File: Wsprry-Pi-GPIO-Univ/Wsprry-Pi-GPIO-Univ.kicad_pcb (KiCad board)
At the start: 2 copper layers, 65 x 30 mm, 25 parts, among them J11 GPIO, J81 Conn_01x04, J82 Conn_01x04, J83 SMA, SW11 Switch, U51 GVA-84

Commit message: Cleanup due to lost libraries
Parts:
- C12, C51: footprint Capacitor_SMD:C_0603_1608Metric -> Wsprry Pi:C_0603_1608Metric
- C52, C53: footprint Capacitor_SMD:C_0402_1005Metric -> Wsprry Pi:C_0402_1005Metric
- C54, C55: footprint Capacitor_SMD:C_0805_2012Metric -> Wsprry Pi:C_0805_2012Metric
- D11: footprint LED_SMD:LED_0603_1608Metric -> Wsprry Pi:LED_0603_1608Metric
- FB11, FB51: footprint Inductor_SMD:L_0603_1608Metric -> Wsprry Pi:L_0603_1608Metric
- J11: footprint Connector_PinSocket_2.54mm:PinSocket_2x20_P2.54mm_Vertical -> Wsprry Pi:PinSocket_2x20_P2.54mm_Vertical
- J81, J82: footprint Connector_PinSocket_2.54mm:PinSocket_1x04_P2.54mm_Vertical -> Wsprry Pi:PinSocket_1x04_P2.54mm_Vertical
- MH1, MH2, MH3, MH4: footprint MountingHole:MountingHole_2.7mm_M2.5 -> Wsprry Pi:MountingHole_2.7mm_M2.5
- R11, R41, R42, R43: footprint Resistor_SMD:R_0603_1608Metric -> Wsprry Pi:R_0603_1608Metric
- R51: footprint Resistor_SMD:R_0805_2012Metric -> Wsprry Pi:R_0805_2012Metric
- U51: footprint Package_TO_SOT_SMD:SOT-89-3 -> Wsprry Pi:SOT-89-3
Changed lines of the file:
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@@
 		)
 		(embedded_fonts no)
-		(model "${KIPRJMOD}/EASYEDA_MODELS/SW-SMD_4P-L5.1-W5.1-P3.70-LS6.5-TL_H1.5.step"
+		(model "${KIPRJMOD}/libraries/3dmodels/vendor/SW-SMD_4P-L5.1-W5.1-P3.70-LS6.5-TL_H1.5.step"
 			(offset
 				(xyz 0 0 0)
@@
 		)
 	)
-	(footprint "LED_SMD:LED_0603_1608Metric"
+	(footprint "Wsprry Pi:LED_0603_1608Metric"
 		(layer "F.Cu")
 		(at 104.6225 77.58)
@@
 		)
 		(embedded_fonts no)
-		(model "${KICAD9_3DMODEL_DIR}/LED_SMD.3dshapes/LED_0603_1608Metric.step"
+		(model "${KIPRJMOD}/libraries/3dmodels/LED_SMD.3dshapes/LED_0603_1608Metric.step"
 			(offset
 				(xyz 0 0 0)
@@
 		)
 	)
-	(footprint "Capacitor_SMD:C_0805_2012Metric"
+	(footprint "Wsprry Pi:C_0805_2012Metric"
 		(layer "F.Cu")
 		(at 146.694973 83.11)
@@
 		)
 		(embedded_fonts no)
-		(model "${KICAD9_3DMODEL_DIR}/Capacitor_SMD.3dshapes/C_0805_2012Metric.step"
+		(model "${KIPRJMOD}/libraries/3dmodels/Capacitor_SMD.3dshapes/C_0805_2012Metric.step"
 			(offset
 				(xyz 0 0 0)
@@
 		)
 	)
-	(footprint "MountingHole:MountingHole_2.7mm_M2.5"
+	(footprint "Wsprry Pi:MountingHole_2.7mm_M2.5"
 		(layer "F.Cu")
 		(at 161.5 73.5)
@@
 		)
 		(embedded_fonts no)
-		(model "${KIPRJMOD}/EASYEDA_MODELS/SMA-TH_5P-L14.5-W6.0-H9.6_BWSMA-KWE-Z001.step"
+		(model "${KIPRJMOD}/libraries/3dmodels/vendor/SMA-TH_5P-L14.5-W6.0-H9.6_BWSMA-KWE-Z001.step"
 			(offset
 				(xyz 4.315 0 -3.5)
@@
 		)
 	)
-	(footprint "Inductor_SMD:L_0603_1608Metric"
+	(footprint "Wsprry Pi:L_0603_1608Metric"
 		(layer "F.Cu")
 		(at 107.581 77.58)
@@
 		)
 		(embedded_fonts no)
-		(model "${KICAD9_3DMODEL_DIR}/Inductor_SMD.3dshapes/L_0603_1608Metric.step"
+		(model "${KIPRJMOD}/libraries/3dmodels/Inductor_SMD.3dshapes/L_0603_1608Metric.step"
 			(offset
 				(xyz 0 0 0)
@@
 		)
 	)
-	(footprint "Capacitor_SMD:C_0402_1005Metric"
+	(footprint "Wsprry Pi:C_0402_1005Metric"
 		(layer "F.Cu")
 		(at 142.88 87.605 90)
@@
 		)
 		(embedded_fonts no)
-		(model "${KICAD9_3DMODEL_DIR}/Capacitor_SMD.3dshapes/C_0402_1005Metric.step"
+		(model "${KIPRJMOD}/libraries/3dmodels/Capacitor_SMD.3dshapes/C_0402_1005Metric.step"
 			(offset
 				(xyz 0 0 0)
@@
 		)
 	)
-	(footprint "Inductor_SMD:L_0603_1608Metric"
+	(footprint "Wsprry Pi:L_0603_1608Metric"
 		(layer "F.Cu")
 		(at 138.5425 88.0875)
@@
 		)
 		(embedded_fonts no)
-		(model "${KICAD9_3DMODEL_DIR}/Inductor_SMD.3dshapes/L_0603_1608Metric.step"
+		(model "${KIPRJMOD}/libraries/3dmodels/Inductor_SMD.3dshapes/L_0603_1608Metric.step"
 			(offset
 				(xyz 0 0 0)
@@
 		)
 	)
-	(footprint "Resistor_SMD:R_0603_1608Metric"
+	(footprint "Wsprry Pi:R_0603_1608Metric"
 		(layer "F.Cu")
 		(at 143.514973 81.648 180)
@@
 		)
 		(embedded_fonts no)
-		(model "${KICAD9_3DMODEL_DIR}/Resistor_SMD.3dshapes/R_0603_1608Metric.step"
+		(model "${KIPRJMOD}/libraries/3dmodels/Resistor_SMD.3dshapes/R_0603_1608Metric.step"
 			(offset
 				(xyz 0 0 0)
@@
 		(embedded_fonts no)
 	)
-	(footprint "Resistor_SMD:R_0805_2012Metric"
+	(footprint "Wsprry Pi:R_0805_2012Metric"
 		(layer "F.Cu")
 		(at 145.04 88.0875)
@@
 		)
 		(embedded_fonts no)
-		(model "${KICAD9_3DMODEL_DIR}/Resistor_SMD.3dshapes/R_0805_2012Metric.step"
+		(model "${KIPRJMOD}/libraries/3dmodels/Resistor_SMD.3dshapes/R_0805_2012Metric.step"
 			(offset
 				(xyz 0 0 0)
@@
 		)
 	)
-	(footprint "MountingHole:MountingHole_2.7mm_M2.5"
+	(footprint "Wsprry Pi:MountingHole_2.7mm_M2.5"
 		(layer "F.Cu")
 		(at 103.5 96.5)
@@
 		(embedded_fonts no)
 	)
-	(footprint "Resistor_SMD:R_0603_1608Metric"
+	(footprint "Wsprry Pi:R_0603_1608Metric"
 		(layer "F.Cu")
 		(at 143.514973 83.109)
@@
 		)
 		(embedded_fonts no)
-		(model "${KICAD9_3DMODEL_DIR}/Resistor_SMD.3dshapes/R_0603_1608Metric.step"
+		(model "${KIPRJMOD}/libraries/3dmodels/Resistor_SMD.3dshapes/R_0603_1608Metric.step"
 			(offset
 				(xyz 0 0 0)
@@
 		)
 	)
-	(footprint "MountingHole:MountingHole_2.7mm_M2.5"
+	(footprint "Wsprry Pi:MountingHole_2.7mm_M2.5"
 		(layer "F.Cu")
 		(at 103.5 73.5)
@@
 		(embedded_fonts no)
 	)
-	(footprint "Resistor_SMD:R_0603_1608Metric"
+	(footprint "Wsprry Pi:R_0603_1608Metric"
 		(layer "F.Cu")
 		(at 141.864973 80.189)
@@
 		)
 		(embedded_fonts no)
-		(model "${KICAD9_3DMODEL_DIR}/Resistor_SMD.3dshapes/R_0603_1608Metric.step"
+		(model "${KIPRJMOD}/libraries/3dmodels/Resistor_SMD.3dshapes/R_0603_1608Metric.step"
 			(offset
 				(xyz 0 0 0)
@@
 		)
 	)
-	(footprint "Capacitor_SMD:C_0603_1608Metric"
+	(footprint "Wsprry Pi:C_0603_1608Metric"
 		(layer "F.Cu")
 		(at 140.7625 87.3125 90)
@@
 		)
 		(embedded_fonts no)
-		(model "${KICAD9_3DMODEL_DIR}/Capacitor_SMD.3dshapes/C_0603_1608Metric.step"
+		(model "${KIPRJMOD}/libraries/3dmodels/Capacitor_SMD.3dshapes/C_0603_1608Metric.step"
 			(offset
 				(xyz 0 0 0)
@@
 		)
 	)
-	(footprint "Package_TO_SOT_SMD:SOT-89-3"
+	(footprint "Wsprry Pi:SOT-89-3"
 		(layer "F.Cu")
 		(at 149.6 86.5875)
@@
 		)
 		(embedded_fonts no)
-		(model "${KICAD9_3DMODEL_DIR}/Package_TO_SOT_SMD.3dshapes/SOT-89-3.step"
+		(model "${KIPRJMOD}/libraries/3dmodels/Package_TO_SOT_SMD.3dshapes/SOT-89-3.step"
 			(offset
 				(xyz 0 0 0)
@@
 		)
 	)
-	(footprint "MountingHole:MountingHole_2.7mm_M2.5"
+	(footprint "Wsprry Pi:MountingHole_2.7mm_M2.5"
 		(layer "F.Cu")
 		(at 161.5 96.5)
@@
 		(embedded_fonts no)
 	)
-	(footprint "Connector_PinSocket_2.54mm:PinSocket_1x04_P2.54mm_Vertical"
+	(footprint "Wsprry Pi:PinSocket_1x04_P2.54mm_Vertical"
 		(layer "F.Cu")
 		(at 144.871658 98.471175 180)
@@
 		)
 		(embedded_fonts no)
-		(model "${KICAD9_3DMODEL_DIR}/Connector_PinSocket_2.54mm.3dshapes/PinSocket_1x04_P2.54mm_Vertical.step"
+		(model "${KIPRJMOD}/libraries/3dmodels/Connector_PinSocket_2.54mm.3dshapes/PinSocket_1x04_P2.54mm_Vertical.step"
 			(offset
 				(xyz 0 0 0)
@@
 		)
 	)
-	(footprint "Capacitor_SMD:C_0402_1005Metric"
+	(footprint "Wsprry Pi:C_0402_1005Metric"
 		(layer "F.Cu")
 		(at 141.96 87.605 90)
@@
 		)
 		(embedded_fonts no)
-		(model "${KICAD9_3DMODEL_DIR}/Capacitor_SMD.3dshapes/C_0402_1005Metric.step"
+		(model "${KIPRJMOD}/libraries/3dmodels/Capacitor_SMD.3dshapes/C_0402_1005Metric.step"
 			(offset
 				(xyz 0 0 0)
@@
 		)
 	)
-	(footprint "Capacitor_SMD:C_0805_2012Metric"
+	(footprint "Wsprry Pi:C_0805_2012Metric"
 		(layer "F.Cu")
 		(at 147.65 90.795 -90)
@@
 		)
 		(embedded_fonts no)
-		(model "${KICAD9_3DMODEL_DIR}/Capacitor_SMD.3dshapes/C_0805_2012Metric.step"
+		(model "${KIPRJMOD}/libraries/3dmodels/Capacitor_SMD.3dshapes/C_0805_2012Metric.step"
 			(offset
 				(xyz 0 0 0)
@@
 		)
 	)
-	(footprint "Resistor_SMD:R_0603_1608Metric"
+	(footprint "Wsprry Pi:R_0603_1608Metric"
 		(layer "F.Cu")
 		(at 101.66 77.58)
@@
 		)
 		(embedded_fonts no)
-		(model "${KICAD9_3DMODEL_DIR}/Resistor_SMD.3dshapes/R_0603_1608Metric.step"
+		(model "${KIPRJMOD}/libraries/3dmodels/Resistor_SMD.3dshapes/R_0603_1608Metric.step"
 			(offset
 				(xyz 0 0 0)
@@
 		)
 	)
-	(footprint "Connector_PinSocket_2.54mm:PinSocket_1x04_P2.54mm_Vertical"
+	(footprint "Wsprry Pi:PinSocket_1x04_P2.54mm_Vertical"
 		(layer "F.Cu")
 		(at 112.851658 98.471175 180)
@@
 		)
 		(embedded_fonts no)
-		(model "${KICAD9_3DMODEL_DIR}/Connector_PinSocket_2.54mm.3dshapes/PinSocket_1x04_P2.54mm_Vertical.step"
+		(model "${KIPRJMOD}/libraries/3dmodels/Connector_PinSocket_2.54mm.3dshapes/PinSocket_1x04_P2.54mm_Vertical.step"
 			(offset
 				(xyz 0 0 0)
@@
 		)
 	)
-	(footprint "Capacitor_SMD:C_0603_1608Metric"
+	(footprint "Wsprry Pi:C_0603_1608Metric"
 		(layer "F.Cu")
 		(at 107.59 79.04 180)
@@
 		)
 		(embedded_fonts no)
-		(model "${KICAD9_3DMODEL_DIR}/Capacitor_SMD.3dshapes/C_0603_1608Metric.step"
+		(model "${KIPRJMOD}/libraries/3dmodels/Capacitor_SMD.3dshapes/C_0603_1608Metric.step"
 			(offset
 				(xyz 0 0 0)
@@
 		)
 	)
-	(footprint "Connector_PinSocket_2.54mm:PinSocket_2x20_P2.54mm_Vertical"
+	(footprint "Wsprry Pi:PinSocket_2x20_P2.54mm_Vertical"
 		(layer "B.Cu")
 		(at 108.37 74.77 -90)
@@
 		)
 		(embedded_fonts no)
-		(model "${KICAD9_3DMODEL_DIR}/Connector_PinSocket_2.54mm.3dshapes/PinSocket_2x20_P2.54mm_Vertical.step"
+		(model "${KIPRJMOD}/libraries/3dmodels/Connector_PinSocket_2.54mm.3dshapes/PinSocket_2x20_P2.54mm_Vertical.step"
 			(offset
 				(xyz 0 0 0)

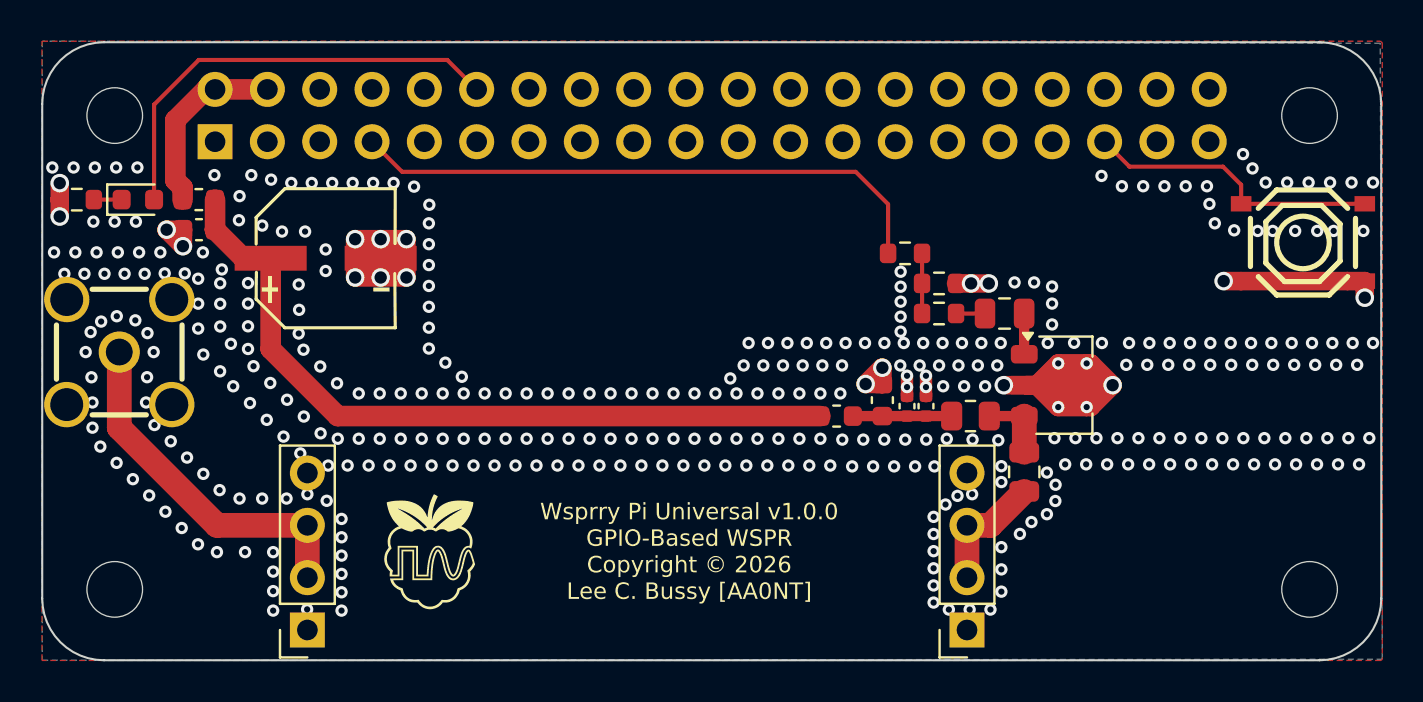
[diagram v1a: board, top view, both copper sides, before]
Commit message: Add GPIO Selector
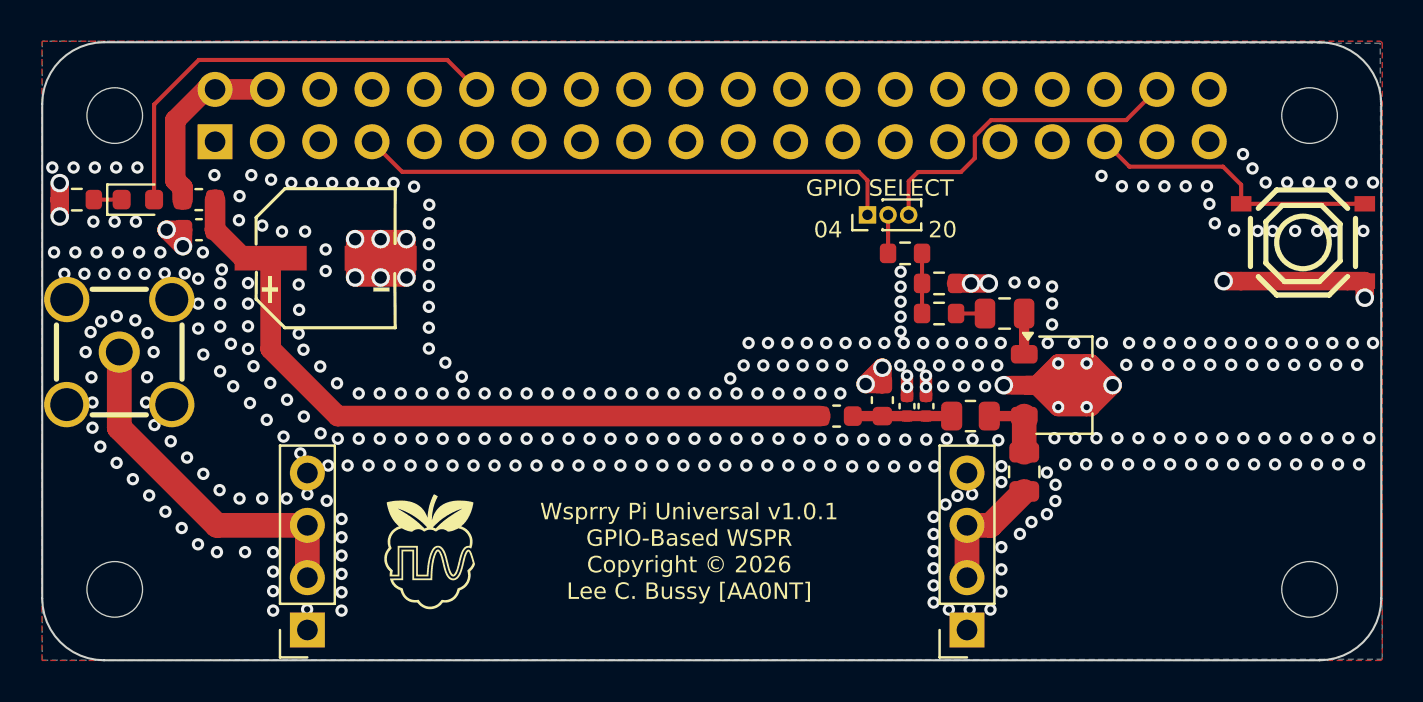
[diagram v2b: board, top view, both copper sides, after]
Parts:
- added J21: GPIO Select, Connector_PinHeader_1.00mm:PinHeader_1x03_P1.00mm_Vertical, F.Cu at (140.0, 78.3)
- C11: value 100µF -> 47µF
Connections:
- J11 pad 38: unconnected-(J11-Pin_38-Pad38) -> /GPIO_CLK20
- J11 pad 7: /GPIO_CLK -> /GPIO_CLK4
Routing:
- net /GPIO_CLK: track 28.7 -> 1.87 mm
- net /GPIO_CLK4: track 0.00 -> 26.5 mm
- net /GPIO_CLK20: track 0.00 -> 16.2 mm
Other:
- board text added: "04"
- board text added: "20"
- board text added: "GPIO SELECT"
- board text added: "Wsprry Pi Universal v1.0.1 GPIO-Based WSPR Copyright © 2026 Lee C. Bussy [AA0NT]"
- board text removed: "Wsprry Pi Universal v1.0.0 GPIO-Based WSPR Copyright © 2026 Lee C. Bussy [AA0NT]"

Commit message: Re-purpose for broadband amp
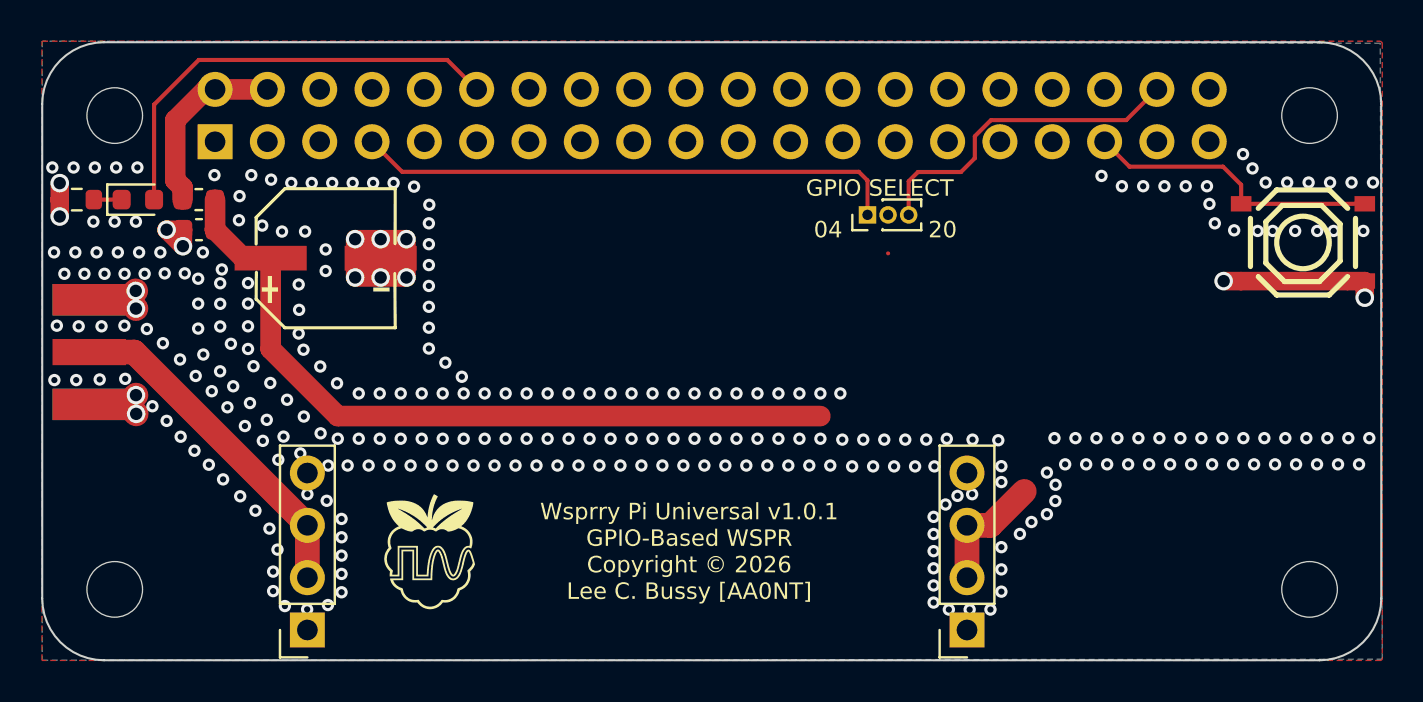
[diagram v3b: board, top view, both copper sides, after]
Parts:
- removed C51: 1µF, Wsprry Pi:C_0603_1608Metric
- removed C52: 100nF, Wsprry Pi:C_0402_1005Metric
- removed C53: 10nF, Wsprry Pi:C_0402_1005Metric
- removed C54, C55: 1uF, Wsprry Pi:C_0805_2012Metric
- removed FB51: 600Ω@100MHz, Wsprry Pi:L_0603_1608Metric
- removed R41, R43: 40.2Ω, Wsprry Pi:R_0603_1608Metric
- removed R42: 10Ω, Wsprry Pi:R_0603_1608Metric
- removed R51: 10Ω, Wsprry Pi:R_0805_2012Metric
- removed U51: GVA-84, Wsprry Pi:SOT-89-3
- J83: value SMA -> SMA_Adafruit_1865; footprint Wsprry Pi:SMA-TH_BWSMA-KWE-Z001 -> Wsprry Pi:SMA_Adafruit_1865_EdgeMount
- moved J83 3.74 mm to (100.0, 85.0), turned to -90 degrees
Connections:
- J83 pad 1: GND -> /RF_OUT
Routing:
- net GND: track 44.3 -> 30.5 mm, vias 378 -> 297
- net Net-(C51-Pad1): track 4.76 -> 0.00 mm
- net /GVA84_BIAS_RF: track 3.42 -> 0.00 mm
- net Net-(R41-Pad2): track 2.92 -> 0.00 mm
- net /GVA84_IN: track 1.98 -> 0.00 mm
- net /GPIO_CLK: track 1.87 -> 0.00 mm
- net /RF_PAD_OUT: track 1.41 -> 0.00 mm
- net /RF_OUT: track 17.3 -> 16.6 mm
